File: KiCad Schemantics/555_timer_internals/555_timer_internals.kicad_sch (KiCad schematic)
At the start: 3 parts

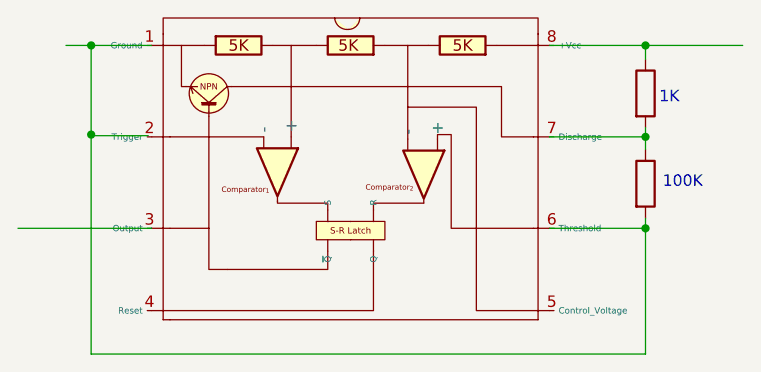
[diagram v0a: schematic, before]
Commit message: DrawIo Diagrams for the D Latch
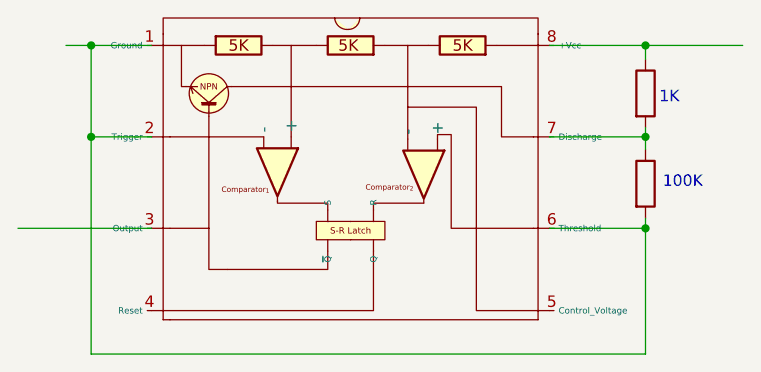
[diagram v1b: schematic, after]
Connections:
- net at U?.1 (Ground): now also R?.2, U?.2 (Trigger), U?.6 (Threshold)
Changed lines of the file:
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@@
   (junction (at 145.034 93.472) (diameter 0) (color 0 0 0 0)
+  )
+  (junction (at 83.439 83.312) (diameter 0) (color 0 0 0 0)
+  )
+  (junction (at 145.034 73.152) (diameter 0) (color 0 0 0 0)
   )
   (junction (at 83.439 73.152) (diameter 0) (color 0 0 0 0)
   )
-  (junction (at 145.034 73.152) (diameter 0) (color 0 0 0 0)
-  )
-  (junction (at 83.439 83.058) (diameter 0) (color 0 0 0 0)
-  )
   (junction (at 145.034 83.312) (diameter 0) (color 0 0 0 0)
-  )
-  (wire (pts (xy 83.439 73.152) (xy 90.17 73.152))
-    (stroke (width 0) (type default) (color 0 0 0 0))
   )
   (wire (pts (xy 145.034 107.442) (xy 145.034 93.472))
     (stroke (width 0) (type default) (color 0 0 0 0))
   )
-  (wire (pts (xy 89.789 83.185) (xy 83.439 83.185))
-    (stroke (width 0) (type default) (color 0 0 0 0))
-  )
-  (wire (pts (xy 83.439 83.058) (xy 83.439 73.152))
+  (wire (pts (xy 83.439 73.152) (xy 83.439 83.312))
     (stroke (width 0) (type default) (color 0 0 0 0))
   )
   (wire (pts (xy 145.034 73.152) (xy 145.034 74.676))
+    (stroke (width 0) (type default) (color 0 0 0 0))
+  )
+  (wire (pts (xy 83.439 83.312) (xy 83.439 107.442))
+    (stroke (width 0) (type default) (color 0 0 0 0))
+  )
+  (wire (pts (xy 83.439 73.152) (xy 90.17 73.152))
     (stroke (width 0) (type default) (color 0 0 0 0))
   )
@@
   )
   (wire (pts (xy 145.034 92.329) (xy 145.034 93.472))
+    (stroke (width 0) (type default) (color 0 0 0 0))
+  )
+  (wire (pts (xy 83.439 83.312) (xy 90.17 83.312))
     (stroke (width 0) (type default) (color 0 0 0 0))
   )
@@
     (stroke (width 0) (type default) (color 0 0 0 0))
   )
-  (wire (pts (xy 83.439 83.185) (xy 83.439 107.442))
-    (stroke (width 0) (type default) (color 0 0 0 0))
-  )

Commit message: Fixed the 555 Timer Internals
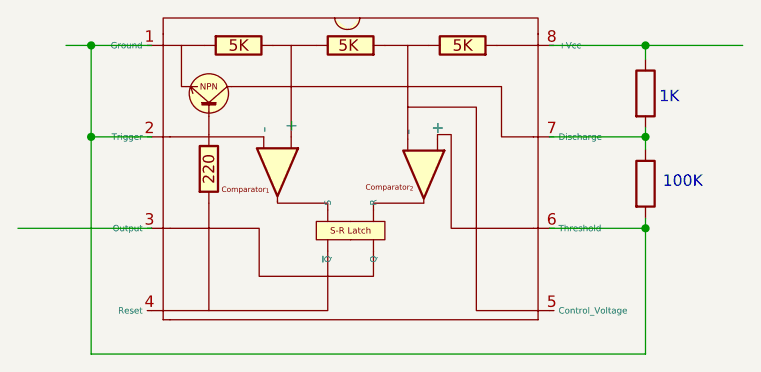
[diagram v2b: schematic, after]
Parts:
- removed U?: 555_Timer_Exploded, symbol Gosheto:555_Timer_Exploded
- added U?: (no value), symbol Gosheto:555_Timer_Exploded
- R?: value (none) -> R
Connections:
- net at R?.2: now also U?.1 (Ground), U?.2 (Trigger), U?.6 (Threshold)
- net at R?.1, R?.2: now also U?.7 (Discharge)
- net at R?.1: now also U?.8 (+Vcc)
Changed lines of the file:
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@@
     (effects (font (size 1.27 1.27)) (justify left bottom))
+  )
+  (symbol (lib_id "Device:R") (at 145.034 78.486 0) (unit 1)
+    (in_bom yes) (on_board yes) (fields_autoplaced)
+    (property "Reference" "R?" (id 0) (at 147.574 77.2159 0)
+      (effects (font (size 1.27 1.27)) (justify left) hide)
+    )
+    (property "Value" "R" (id 1) (at 147.574 79.7559 0)
+      (effects (font (size 1.27 1.27)) (justify left) hide)
+    )
+    (property "Footprint" "" (id 2) (at 143.256 78.486 90)
+      (effects (font (size 1.27 1.27)) hide)
+    )
+    (property "Datasheet" "~" (id 3) (at 145.034 78.486 0)
+      (effects (font (size 1.27 1.27)) hide)
+    )
+    (pin "1")
+    (pin "2")
   )
   (symbol (lib_id "Gosheto:555_Timer_Exploded") (at 112.014 64.77 0) (unit 1)
@@
       (effects (font (size 1.27 1.27)) (justify left) hide)
     )
-    (property "Value" "555_Timer_Exploded" (id 1) (at 122.0471 67.31 0)
+    (property "Value" "" (id 1) (at 122.0471 67.31 0)
       (effects (font (size 1.27 1.27)) (justify left) hide)
     )
@@
       (effects (font (size 1.27 1.27)) hide)
     )
+    (pin "")
+    (pin "")
     (pin "")
     (pin "")
@@
     (pin "8")
   )
-  (symbol (lib_id "Device:R") (at 145.034 78.486 0) (unit 1)
-    (in_bom yes) (on_board yes) (fields_autoplaced)
-    (property "Reference" "R?" (id 0) (at 147.574 77.2159 0)
-      (effects (font (size 1.27 1.27)) (justify left) hide)
-    )
-    (property "Value" "" (id 1) (at 147.574 79.7559 0)
-      (effects (font (size 1.27 1.27)) (justify left) hide)
-    )
-    (property "Footprint" "" (id 2) (at 143.256 78.486 90)
-      (effects (font (size 1.27 1.27)) hide)
-    )
-    (property "Datasheet" "~" (id 3) (at 145.034 78.486 0)
-      (effects (font (size 1.27 1.27)) hide)
-    )
-    (pin "1")
-    (pin "2")
-  )
   (symbol (lib_id "Device:R") (at 145.034 88.519 0) (unit 1)
     (in_bom yes) (on_board yes) (fields_autoplaced)
@@
       (reference "R?") (unit 1) (value "R") (footprint "")
     )
-    (path "/21a4e5f9-158c-4a1e-a6d3-12c826291e62"
+    (path "/2e531d27-fc0f-4094-a6f3-3ee3440c3aa4"
       (reference "U?") (unit 1) (value "555_Timer_Exploded") (footprint "")
     )
